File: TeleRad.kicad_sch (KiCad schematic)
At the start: 8 parts, among them M1 Stepper_Motor_bipolar, M2 Stepper_Motor_bipolar

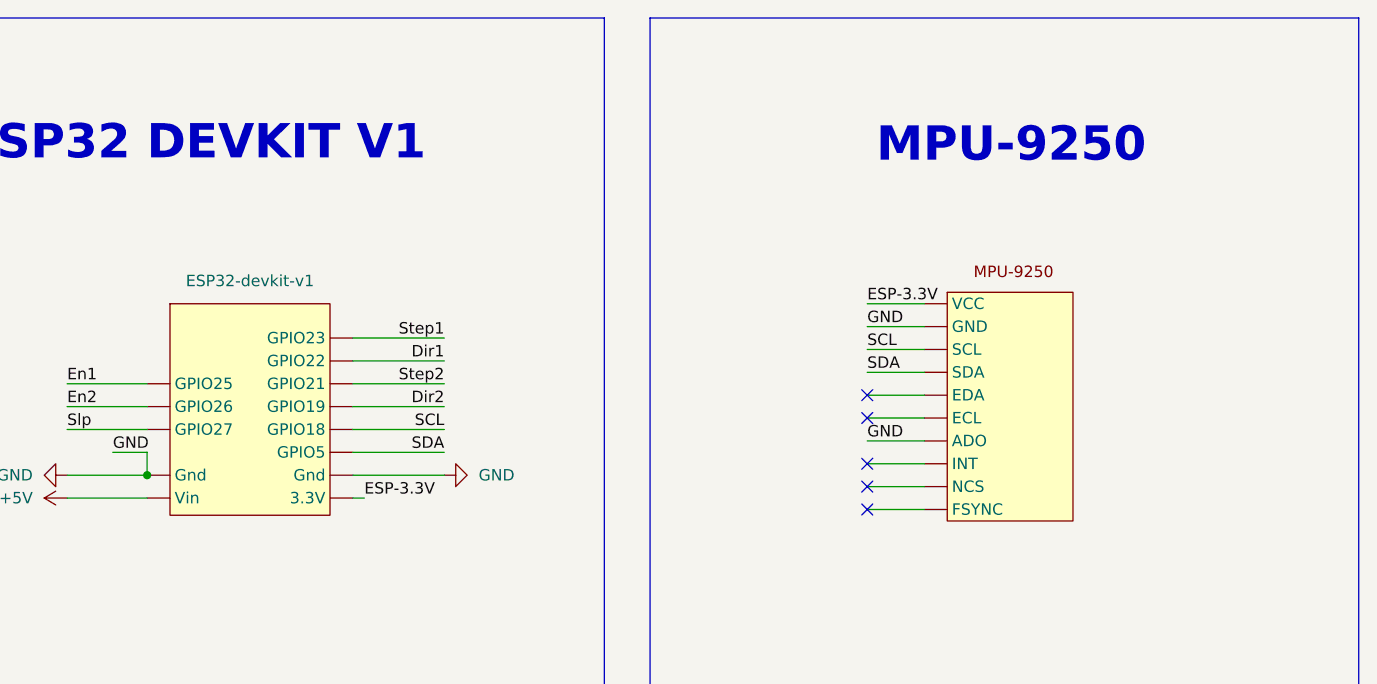
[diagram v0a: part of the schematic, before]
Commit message: Added wiring for Limiting Switches,remved MPU9250
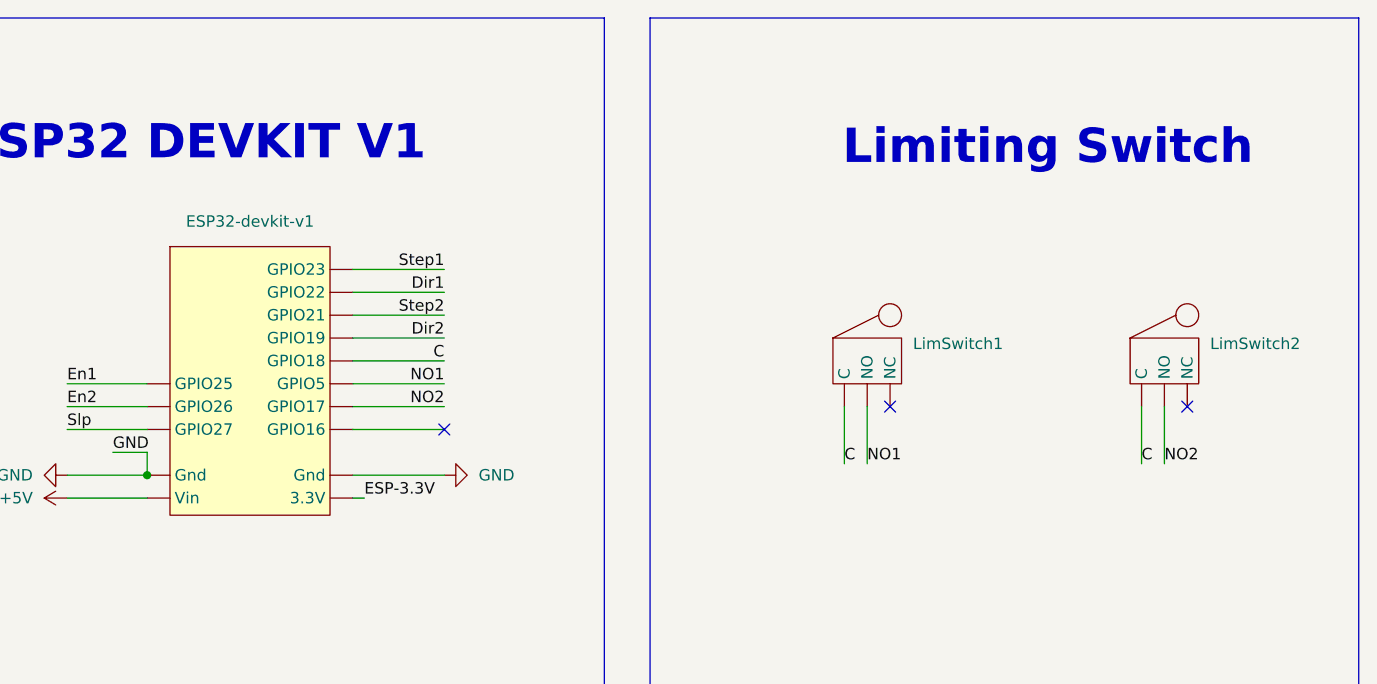
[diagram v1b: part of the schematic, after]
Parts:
- removed U1: (no value), symbol Sensor_Motion:MPU-9250
- added LimSwitch1, LimSwitch2: (no value), symbol Switch:Limiting_Switch
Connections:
- net SCL is gone; now on net Step2: ESP32-devkit-v1. (3.3V)
- net SDA is gone; now on net Step2: ESP32-devkit-v1. (3.3V)
- new net C: ESP32-devkit-v1. (3.3V), LimSwitch1. (NC), LimSwitch2. (NC)
- new net NO1: ESP32-devkit-v1. (3.3V), LimSwitch1. (NC)
- new net NO2: ESP32-devkit-v1. (3.3V), LimSwitch2. (NC)
- no-connect marks 11 -> 9
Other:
- note added: "Limiting Switch"
- note removed: "MPU-9250"
